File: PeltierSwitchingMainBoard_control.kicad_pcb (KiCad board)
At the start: 2 copper layers, 24.6 x 45.1 mm, 24 parts, among them J3 Molex Micro Lock (1.25mm 1.5A), J4 Conn_01x14, U1 HIP4080A

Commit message: Updated silkscreen
Signed-off-by: bebenlebricolo <benoittarrade@hotmail.fr>
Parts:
- removed TP8: TestPoint, TestPoint:TestPoint_Pad_D2.0mm
- added OUT: TestPoint, TestPoint:TestPoint_Pad_D2.0mm, F.Cu at (73.0, 79.4)
- renumbered TP5 to AHB, TP4 to AHO, TP3 to ALO, TP6 to BHB, TP1 to BHO, TP2 to BLO, TP7 to VSENSE
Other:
- board text added: "Power On Led"
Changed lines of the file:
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@@
   (general
     (thickness 1.6)
-    (drawings 8)
+    (drawings 10)
     (tracks 359)
     (zones 0)
@@
   (module PeltierSwitchingMainBoard_control:Molex_MicroLock_1.25_01x06 (layer F.Cu)
     (at 78.105 41.91 180)
-    (fp_text reference J3 (at 4.25 -8.5 180) (layer F.SilkS)
+    (fp_text reference J3 (at -6.096 0.254 180) (layer F.SilkS)
       (effects (font (size 1 1) (thickness 0.15)))
     )
@@
   (module PeltierSwitchingMainBoard_control:Mezzanine_board_14contacts locked (layer F.Cu)
     (at 61.684999 82.185)
-    (fp_text reference J4 (at 1.942001 -1.921) (layer F.SilkS)
+    (fp_text reference J4 (at 1.942001 -1.921) (layer F.SilkS) hide
       (effects (font (size 1 1) (thickness 0.15)))
     )
@@
     (tags "SOIC SO")
     (attr smd)
-    (fp_text reference U1 (at 0 -7.35 90) (layer F.SilkS)
+    (fp_text reference U1 (at 3.556 -7.366 90) (layer F.SilkS)
       (effects (font (size 1 1) (thickness 0.15)))
     )
@@
     (tags "test point SMD pad")
     (attr virtual)
-    (fp_text reference TP8 (at 0 -1.998) (layer F.SilkS)
-      (effects (font (size 1 1) (thickness 0.15)))
+    (fp_text reference OUT (at 1.651 -1.397) (layer F.SilkS)
+      (effects (font (size 0.7 0.7) (thickness 0.1)))
     )
     (fp_text value TestPoint (at 0 2.05) (layer F.Fab)
@@
     (tags "test point SMD pad")
     (attr virtual)
-    (fp_text reference TP7 (at 0 -1.998) (layer F.SilkS)
-      (effects (font (size 1 1) (thickness 0.15)))
+    (fp_text reference VSENSE (at 0 -1.998) (layer F.SilkS)
+      (effects (font (size 0.7 0.7) (thickness 0.1)))
     )
     (fp_text value TestPoint (at 0 2.05) (layer F.Fab)
@@
     (tags "test point SMD pad")
     (attr virtual)
-    (fp_text reference TP6 (at 0 -1.998) (layer F.SilkS)
-      (effects (font (size 1 1) (thickness 0.15)))
+    (fp_text reference BHB (at 0 -1.998) (layer F.SilkS)
+      (effects (font (size 0.7 0.7) (thickness 0.1)))
     )
     (fp_text value TestPoint (at 0 2.05) (layer F.Fab)
@@
     (tags "test point SMD pad")
     (attr virtual)
-    (fp_text reference TP5 (at 0 -1.998) (layer F.SilkS)
-      (effects (font (size 1 1) (thickness 0.15)))
+    (fp_text reference AHB (at 0 -1.998) (layer F.SilkS)
+      (effects (font (size 0.7 0.7) (thickness 0.1)))
     )
     (fp_text value TestPoint (at 0 2.05) (layer F.Fab)
@@
     (tags "test point SMD pad")
     (attr virtual)
-    (fp_text reference TP4 (at 0 -1.998) (layer F.SilkS)
-      (effects (font (size 1 1) (thickness 0.15)))
+    (fp_text reference AHO (at 2.413 -0.127 90) (layer F.SilkS)
+      (effects (font (size 0.7 0.7) (thickness 0.1)))
     )
     (fp_text value TestPoint (at 0 2.05) (layer F.Fab)
@@
     (tags "test point SMD pad")
     (attr virtual)
-    (fp_text reference TP3 (at 0 -1.998) (layer F.SilkS)
-      (effects (font (size 1 1) (thickness 0.15)))
+    (fp_text reference ALO (at -2.159 0.127 90) (layer F.SilkS)
+      (effects (font (size 0.7 0.7) (thickness 0.1)))
     )
     (fp_text value TestPoint (at 0 2.05) (layer F.Fab)
@@
     (tags "test point SMD pad")
     (attr virtual)
-    (fp_text reference TP2 (at 0 -1.998) (layer F.SilkS)
-      (effects (font (size 1 1) (thickness 0.15)))
+    (fp_text reference BLO (at 2.159 0.127 90) (layer F.SilkS)
+      (effects (font (size 0.7 0.7) (thickness 0.1)))
     )
     (fp_text value TestPoint (at 0 2.05) (layer F.Fab)
@@
     (tags "test point SMD pad")
     (attr virtual)
-    (fp_text reference TP1 (at 0 -1.998) (layer F.SilkS)
-      (effects (font (size 1 1) (thickness 0.15)))
+    (fp_text reference BHO (at 0 -1.998) (layer F.SilkS)
+      (effects (font (size 0.7 0.7) (thickness 0.1)))
     )
     (fp_text value TestPoint (at 0 2.05) (layer F.Fab)
@@
     (tags "resistor handsolder")
     (attr smd)
-    (fp_text reference R7 (at 0 -1.82) (layer F.SilkS)
+    (fp_text reference R7 (at -3.81 0) (layer F.SilkS)
       (effects (font (size 1 1) (thickness 0.15)))
     )
@@
     (tags "resistor handsolder")
     (attr smd)
-    (fp_text reference R5 (at 0 -1.82) (layer F.SilkS)
-      (effects (font (size 1 1) (thickness 0.15)))
+    (fp_text reference R5 (at -1.397 -1.651) (layer F.SilkS)
+      (effects (font (size 0.7 0.7) (thickness 0.1)))
     )
     (fp_text value 10k (at 0 1.82) (layer F.Fab)
@@
     (tags "resistor handsolder")
     (attr smd)
-    (fp_text reference R4 (at 0 -1.82) (layer F.SilkS)
+    (fp_text reference R4 (at -3.556 0) (layer F.SilkS)
       (effects (font (size 1 1) (thickness 0.15)))
     )
@@
     (tags "resistor handsolder")
     (attr smd)
-    (fp_text reference R3 (at 0 -1.82) (layer F.SilkS)
+    (fp_text reference R3 (at -3.81 0) (layer F.SilkS)
       (effects (font (size 1 1) (thickness 0.15)))
     )
@@
     (tags "resistor handsolder")
     (attr smd)
-    (fp_text reference R2 (at 0 -1.82) (layer F.SilkS)
+    (fp_text reference R2 (at -4.826 -0.254) (layer F.SilkS)
       (effects (font (size 1 1) (thickness 0.15)))
     )
@@
     (tags "resistor handsolder")
     (attr smd)
-    (fp_text reference R1 (at 0 -1.82) (layer F.SilkS)
+    (fp_text reference R1 (at -0.762 -1.778) (layer F.SilkS)
       (effects (font (size 1 1) (thickness 0.15)))
     )
@@
     (tags "LED handsolder")
     (attr smd)
-    (fp_text reference D3 (at 0 -1.65) (layer F.SilkS)
+    (fp_text reference D3 (at -3.556 0) (layer F.SilkS)
       (effects (font (size 1 1) (thickness 0.15)))
     )
@@
     (tags SOD-123)
     (attr smd)
-    (fp_text reference D2 (at 0 -2 90) (layer F.SilkS)
+    (fp_text reference D2 (at -0.254 1.778 270) (layer F.SilkS)
       (effects (font (size 1 1) (thickness 0.15)))
     )
@@
     (tags SOD-123)
     (attr smd)
-    (fp_text reference D1 (at 0 -2 90) (layer F.SilkS)
+    (fp_text reference D1 (at -0.127 2.159 180) (layer F.SilkS)
       (effects (font (size 1 1) (thickness 0.15)))
     )
@@
     (tags "capacitor handsolder")
     (attr smd)
-    (fp_text reference C8 (at 0 -1.85 90) (layer F.SilkS)
+    (fp_text reference C8 (at -0.254 2.159 180) (layer F.SilkS)
       (effects (font (size 1 1) (thickness 0.15)))
     )
@@
     (tags "capacitor handsolder")
     (attr smd)
-    (fp_text reference C7 (at 0 -1.85 90) (layer F.SilkS)
+    (fp_text reference C7 (at 0 -1.524 90) (layer F.SilkS)
       (effects (font (size 1 1) (thickness 0.15)))
     )
@@
     (tags "capacitor handsolder")
     (attr smd)
-    (fp_text reference C6 (at 0 -1.85) (layer F.SilkS)
+    (fp_text reference C6 (at -3.683 -0.254) (layer F.SilkS)
       (effects (font (size 1 1) (thickness 0.15)))
     )
@@
     )
   )
+  (gr_circle (center 66.802 72.136) (end 67.056 72.39) (layer F.SilkS) (width 0.12))
+  (gr_text "Power On Led" (at 66.294 57.658) (layer F.SilkS)
+    (effects (font (size 0.7 0.7) (thickness 0.1)))
+  )
   (gr_line (start 64.643 81.915) (end 84.201 81.915) (layer Edge.Cuts) (width 0.05))

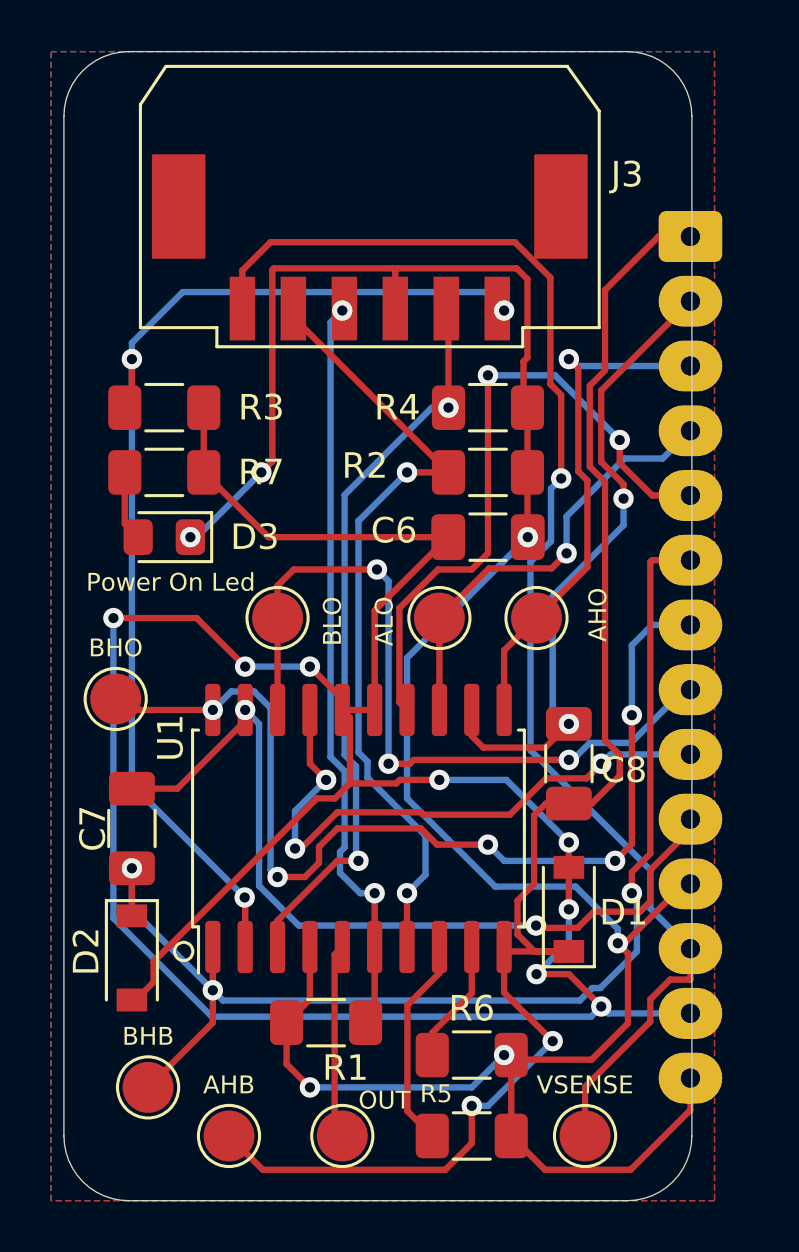
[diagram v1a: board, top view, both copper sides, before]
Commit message: Removed castellated holes (too costy)
Signed-off-by: bebenlebricolo <benoittarrade@hotmail.fr>
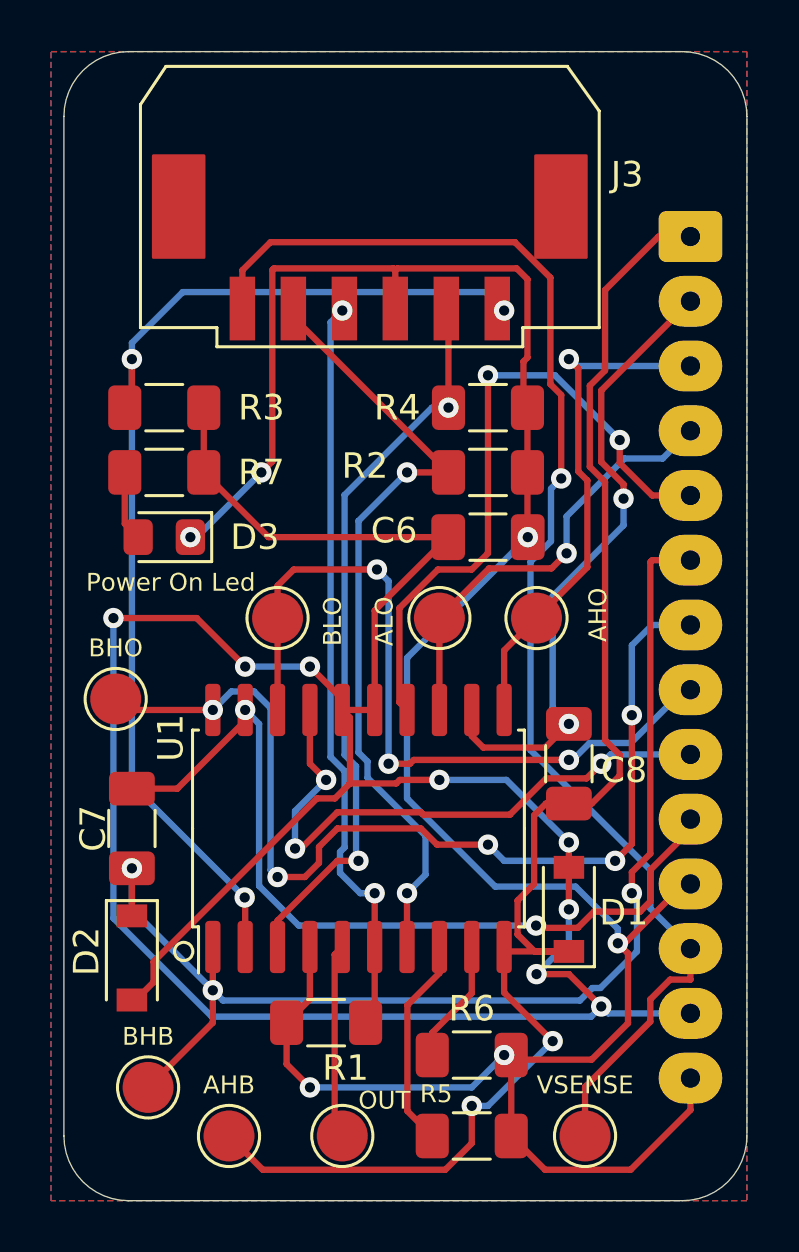
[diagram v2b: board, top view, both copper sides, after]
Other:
- board size 24.6 x 45.1 mm -> 26.8 x 45.1 mm
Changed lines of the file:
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@@
     (effects (font (size 0.7 0.7) (thickness 0.1)))
   )
-  (gr_line (start 64.643 81.915) (end 84.201 81.915) (layer Edge.Cuts) (width 0.05))
+  (gr_line (start 64.643 81.915) (end 86.36 81.915) (layer Edge.Cuts) (width 0.05))
   (gr_line (start 62.103 39.37) (end 62.103 79.375) (layer Edge.Cuts) (width 0.05))
-  (gr_line (start 86.741 39.37) (end 86.741 79.375) (layer Edge.Cuts) (width 0.05))
-  (gr_arc (start 84.201 79.375) (end 84.201 81.915) (angle -90) (layer Edge.Cuts) (width 0.05))
+  (gr_line (start 88.9 39.37) (end 88.9 79.375) (layer Edge.Cuts) (width 0.05))
+  (gr_arc (start 86.36 79.375) (end 86.36 81.915) (angle -90) (layer Edge.Cuts) (width 0.05))
   (gr_arc (start 64.643 79.375) (end 62.103 79.375) (angle -90) (layer Edge.Cuts) (width 0.05))
   (gr_arc (start 64.643 39.37) (end 64.643 36.83) (angle -90) (layer Edge.Cuts) (width 0.05))
-  (gr_arc (start 84.201 39.37) (end 86.741 39.37) (angle -90) (layer Edge.Cuts) (width 0.05))
-  (gr_line (start 64.643 36.83) (end 84.201 36.83) (layer Edge.Cuts) (width 0.05))
+  (gr_arc (start 86.36 39.37) (end 88.9 39.37) (angle -90) (layer Edge.Cuts) (width 0.05))
+  (gr_line (start 64.643 36.83) (end 86.36 36.83) (layer Edge.Cuts) (width 0.05))
   (segment (start 71.755 74.015) (end 71.755 71.96) (width 0.25) (layer F.Cu) (net 1))
   (segment (start 70.84 74.93) (end 71.755 74.015) (width 0.25) (layer F.Cu) (net 1))
@@
     (polygon
       (pts
-        (xy 87.63 81.915) (xy 61.595 81.915) (xy 61.595 36.83) (xy 87.63 36.83)
+        (xy 88.9 81.915) (xy 61.595 81.915) (xy 61.595 36.83) (xy 88.9 36.83)
       )
     )
@@
     (polygon
       (pts
-        (xy 87.63 81.915) (xy 61.595 81.915) (xy 61.595 36.83) (xy 87.63 36.83)
+        (xy 88.9 81.915) (xy 61.595 81.915) (xy 61.595 36.83) (xy 88.9 36.83)
       )
     )

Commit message: Removed custom footprint
Signed-off-by: bebenlebricolo <benoittarrade@hotmail.fr>
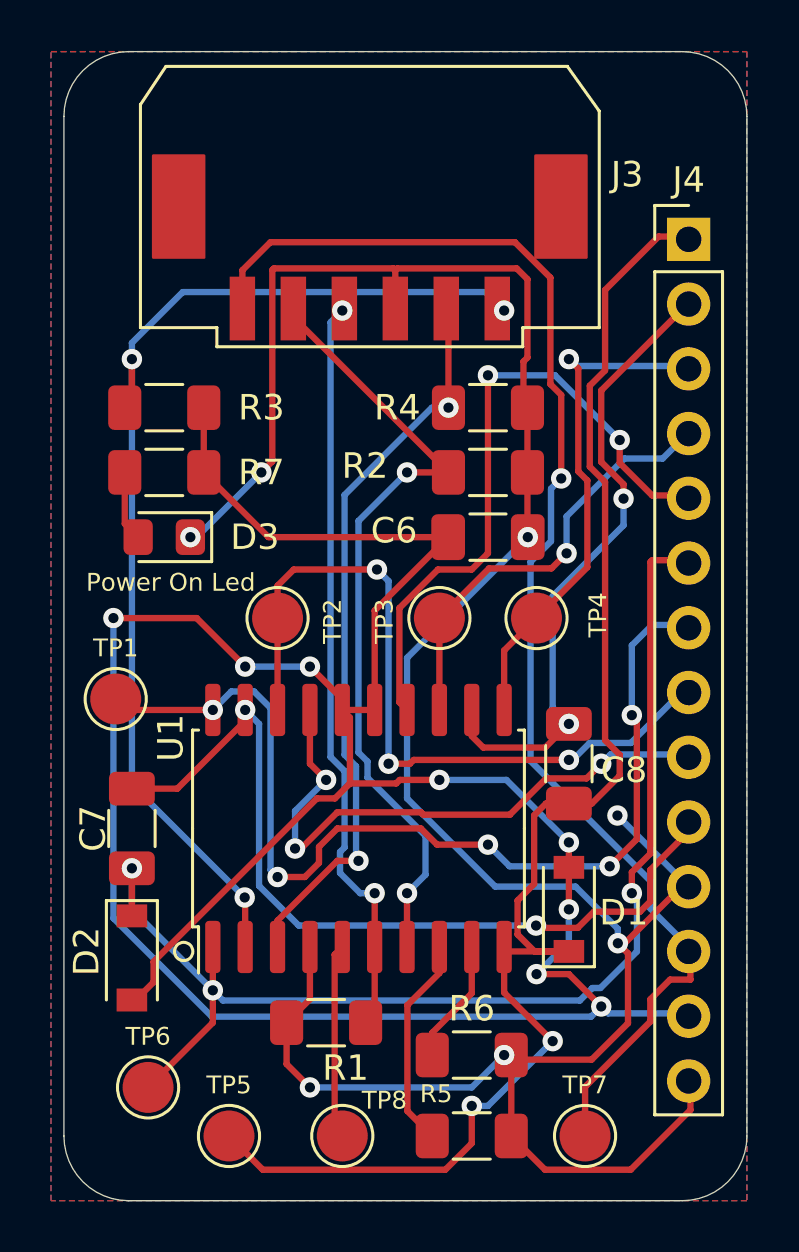
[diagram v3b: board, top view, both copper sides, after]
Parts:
- J4: footprint PeltierSwitchingMainBoard_control:Mezzanine_board_14contacts -> Connector_PinHeader_2.54mm:PinHeader_1x14_P2.54mm_Vertical
- moved J4 45.4 mm to (86.6, 44.2)
- renumbered BHO to TP1, BLO to TP2, ALO to TP3, AHO to TP4, AHB to TP5, BHB to TP6, VSENSE to TP7, OUT to TP8
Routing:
- net +12V: track 103.4 -> 107.6 mm, vias 8 -> 9

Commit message: Updated silkscreen and exported Gerber files
Signed-off-by: bebenlebricolo <benoittarrade@hotmail.fr>
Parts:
- removed TP7: TestPoint, TestPoint:TestPoint_Pad_D2.0mm
- added VSense: TestPoint, TestPoint:TestPoint_Pad_D2.0mm, F.Cu at (83.1, 78.0)
- renumbered TP5 to AHB, TP4 to AHO, TP3 to ALO, TP6 to BHB, TP1 to BHO, TP2 to BLO, TP8 to OUT
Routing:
- net GND: track 97.2 -> 82.2 mm, vias 6 -> 8
- net /IN-: track 31.4 -> 34.2 mm
- net /HEN: track 43.6 -> 40.9 mm
- net /VSense: track 53.7 -> 52.1 mm
- net /Disable: track 29.2 -> 30.0 mm
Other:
- board text added: "Beer Thermoregulation System main board (control) V1"
- board text added: "Control board V1"
- board text added: "Designed by Benoit Tarrade (alias bebenlebricolo) https://github.com/bebenlebricolo"
